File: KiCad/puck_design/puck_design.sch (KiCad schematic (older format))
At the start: 2 parts

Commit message: Changed library name
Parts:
- removed U?: ITG-3701, symbol library:ITG-3701
- removed U?: TE832-M1, symbol library:TE832-M1
- added U?: ITG-3701, symbol puck_library:ITG-3701
- added U?: TE832-M1, symbol puck_library:TE832-M1
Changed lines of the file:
@@
 EESchema Schematic File Version 4
+LIBS:puck_design-cache
 EELAYER 26 0
 EELAYER END
@@
 $EndDescr
 $Comp
-L library:ITG-3701 U?
-U 1 1 5BF4969E
-P 3500 3400
-F 0 "U?" H 4241 3496 50  0000 L CNN
-F 1 "ITG-3701" H 4241 3405 50  0000 L CNN
-F 2 "" H 3500 3400 50  0001 C CNN
-F 3 "" H 3500 3400 50  0001 C CNN
-	1    3500 3400
+L puck_library:ITG-3701 U?
+U 1 1 5BF49DCF
+P 3550 3200
+F 0 "U?" H 4291 3296 50  0000 L CNN
+F 1 "ITG-3701" H 4291 3205 50  0000 L CNN
+F 2 "" H 3550 3200 50  0001 C CNN
+F 3 "" H 3550 3200 50  0001 C CNN
+	1    3550 3200
 	1    0    0    -1
 $EndComp
 $Comp
-L library:TE832-M1 U?
-U 1 1 5BF496E3
-P 6000 3250
-F 0 "U?" H 5525 3565 50  0000 C CNN
-F 1 "TE832-M1" H 5525 3474 50  0000 C CNN
-F 2 "" H 5550 3550 50  0001 C CNN
-F 3 "" H 5550 3550 50  0001 C CNN
-	1    6000 3250
+L puck_library:TE832-M1 U?
+U 1 1 5BF49E68
+P 6000 3100
+F 0 "U?" H 5525 3415 50  0000 C CNN
+F 1 "TE832-M1" H 5525 3324 50  0000 C CNN
+F 2 "" H 5550 3400 50  0001 C CNN
+F 3 "" H 5550 3400 50  0001 C CNN
+	1    6000 3100
 	1    0    0    -1
 $EndComp

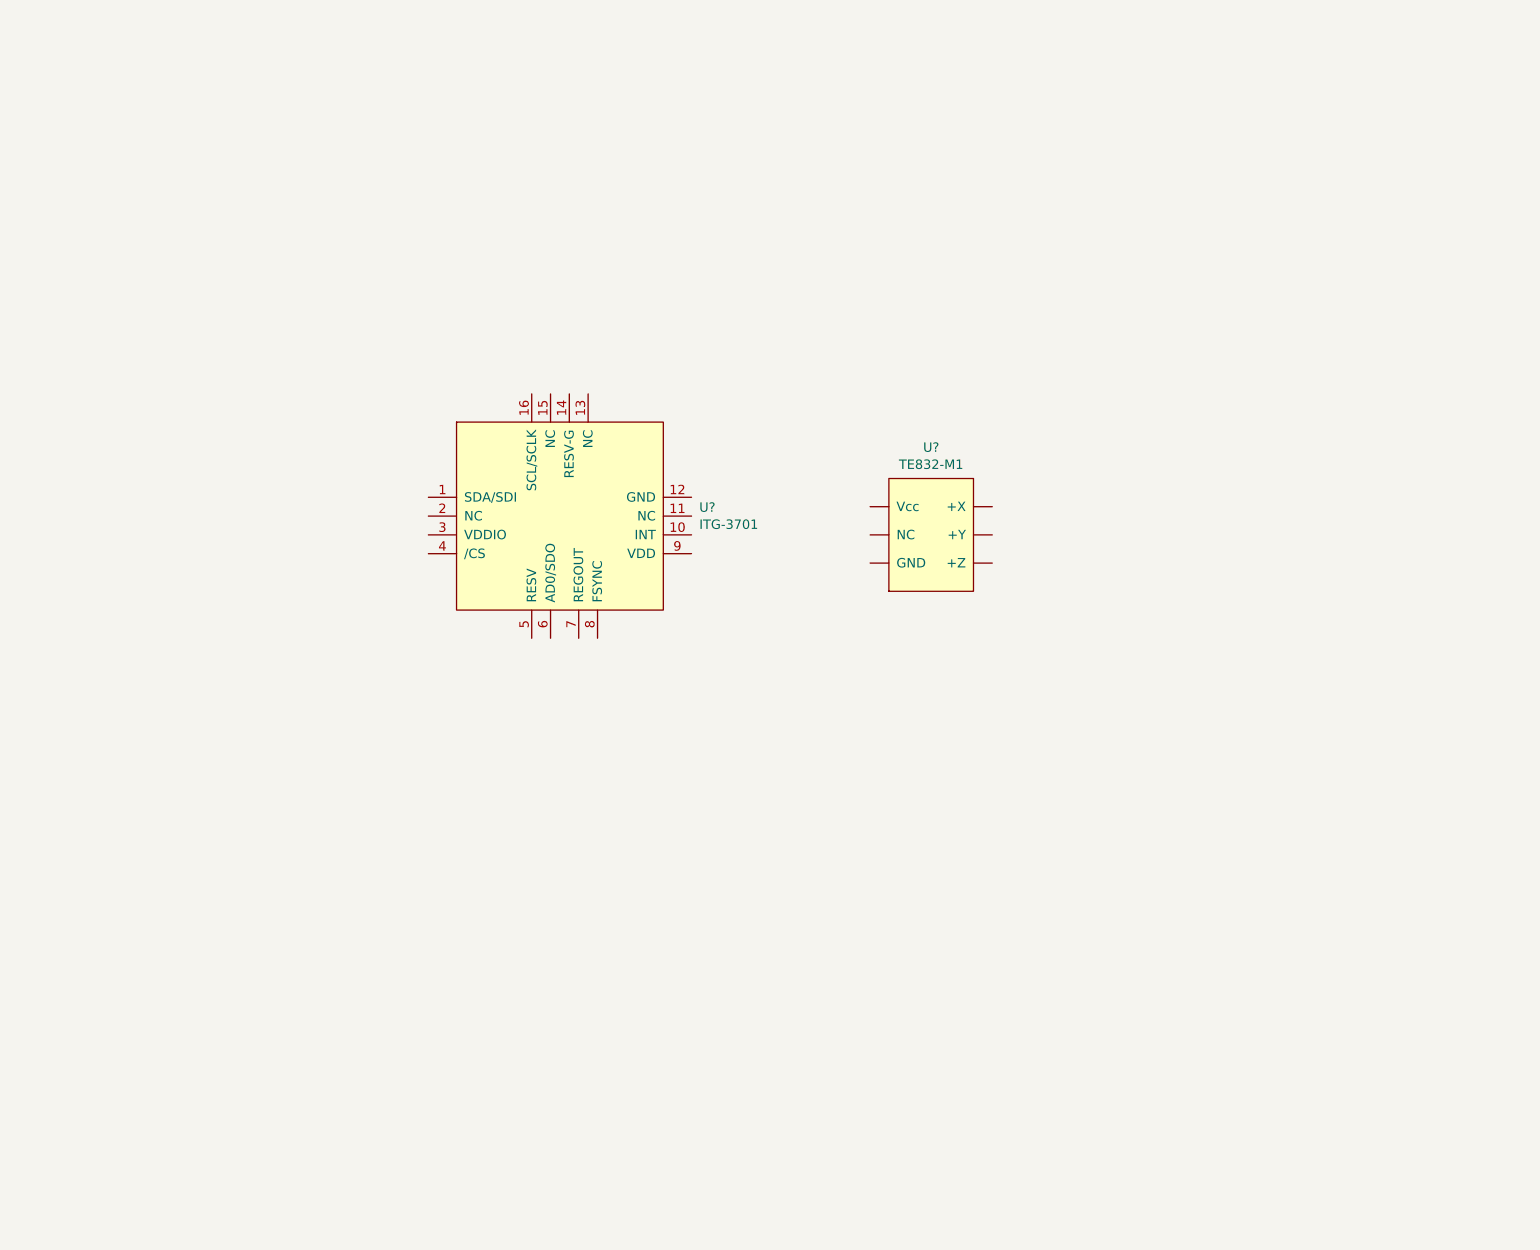
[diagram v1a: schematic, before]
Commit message: added connections according to config no 4
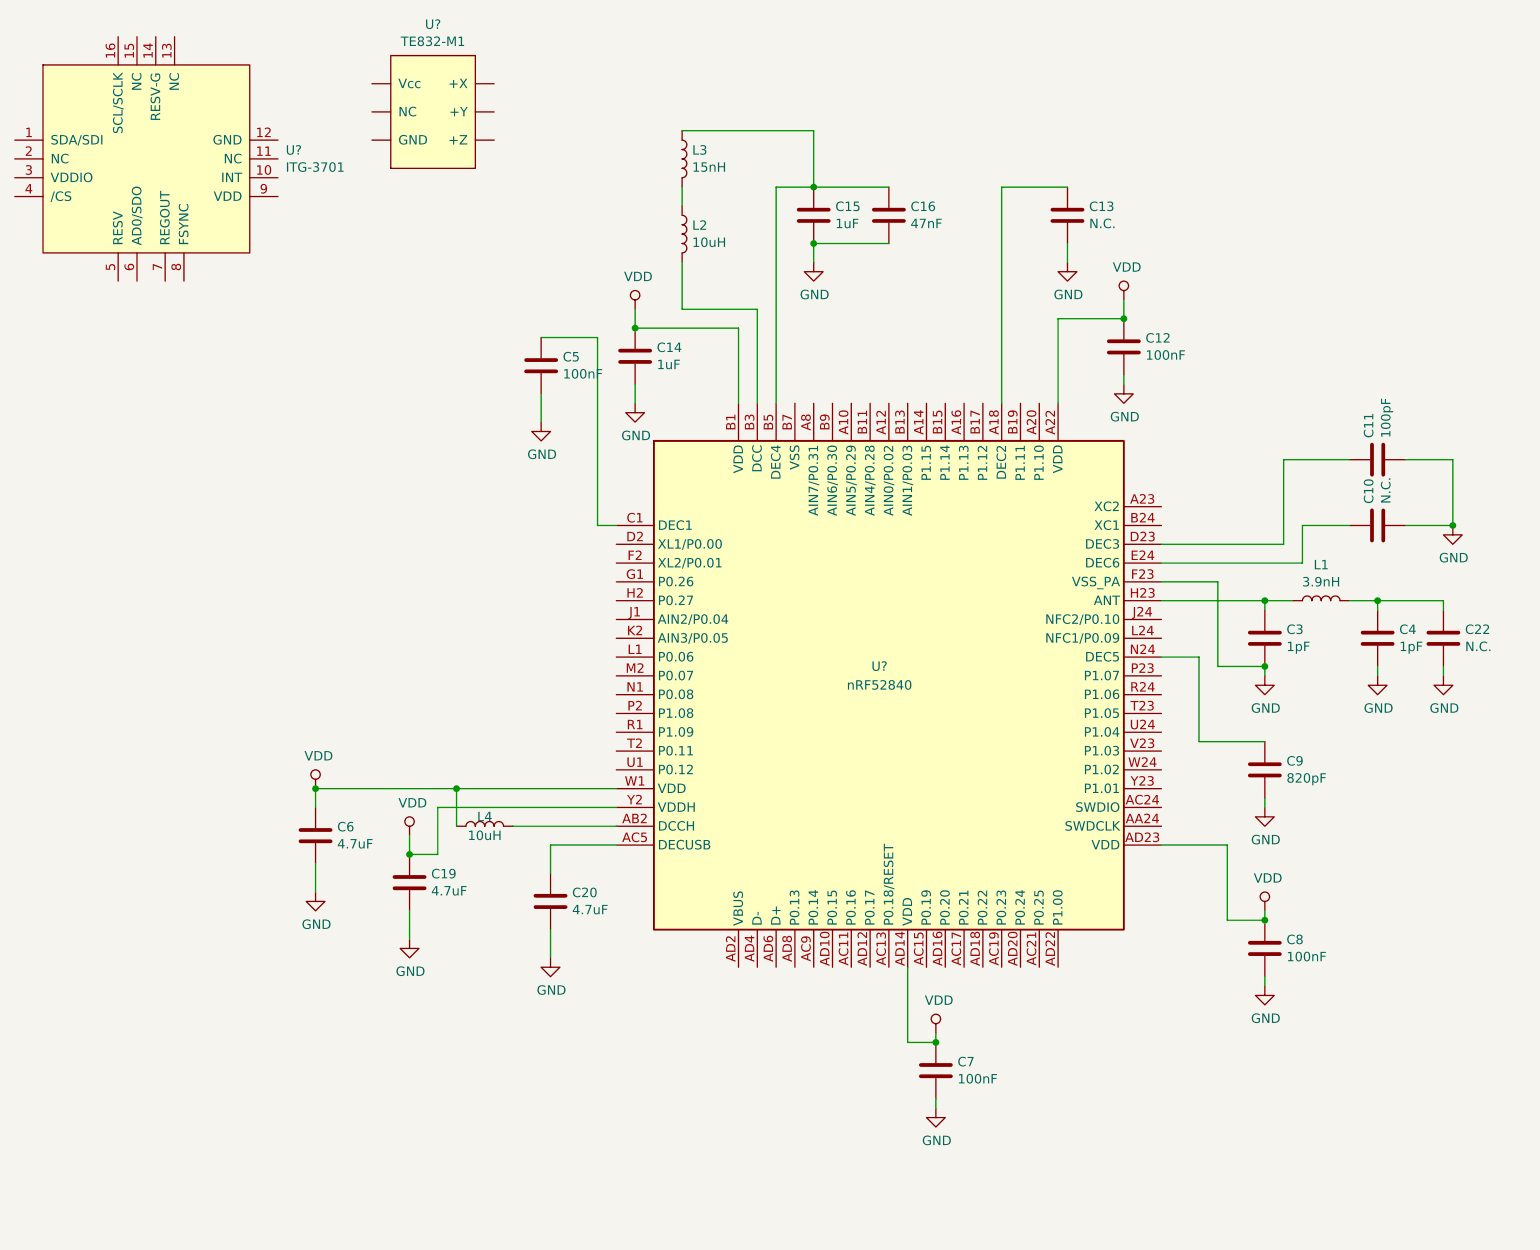
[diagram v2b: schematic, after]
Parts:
- added C10, C13, C22: N.C., symbol Device:C
- added C11: 100pF, symbol Device:C
- added C12, C5, C7, C8: 100nF, symbol Device:C
- added C14, C15: 1uF, symbol Device:C
- added C16: 47nF, symbol Device:C
- added C19, C20, C6: 4.7uF, symbol Device:C
- added C3, C4: 1pF, symbol Device:C
- added C9: 820pF, symbol Device:C
- added L1: 3.9nH, symbol Device:L
- added L2, L4: 10uH, symbol Device:L
- added L3: 15nH, symbol Device:L
- added U?: nRF52840, Package_DFN_QFN:Nordic_AQFN-73-1EP_7x7mm_P0.5mm, symbol puck_library:nRF52840
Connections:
- new net: C13.1, U?.A18 (DEC2)
- new net: L4.2, U?.AB2 (DCCH)
- new net: C20.1, U?.AC5 (DECUSB)
- new net: L2.2, U?.B3 (DCC)
- new net: C15.1, C16.1, L3.1, U?.B5 (DEC4)
- new net: C5.1, U?.C1 (DEC1)
- new net: C11.1, U?.D23 (DEC3)
- new net: C10.1, U?.E24 (DEC6)
- new net: C3.1, L1.1, U?.H23 (ANT)
- new net: C9.1, U?.N24 (DEC5)
- new net: C22.1, C4.1, L1.2
- new net: L2.1, L3.2
- new net GND: C10.2, C11.2, C12.2, C13.2, C14.2, C15.2, C16.2, C19.2, C20.2, C22.2, C3.2, C4.2, C5.2, C6.2, C7.2, C8.2, C9.2, U?.F23 (VSS_PA)
- new net VDD: C12.1, C14.1, C19.1, C6.1, C7.1, C8.1, L4.1, U?.A22 (VDD), U?.AD14 (VDD), U?.AD23 (VDD), U?.B1 (VDD), U?.W1 (VDD), U?.Y2 (VDDH)
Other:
- moved on the sheet: U?

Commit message: corrected errors
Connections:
- net GND: now also U?.B7 (VSS)
- net at C15.1, C16.1, L3.1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: now also C10.1, U?.E24 (DEC6)
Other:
- moved on the sheet: C11, C22
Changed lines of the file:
@@
 L Device:C C22
 U 1 1 5BF5900D
-P 8250 3800
-F 0 "C22" H 8365 3846 50  0000 L CNN
-F 1 "N.C." H 8365 3755 50  0000 L CNN
-F 2 "" H 8288 3650 50  0001 C CNN
-F 3 "~" H 8250 3800 50  0001 C CNN
-	1    8250 3800
+P 8350 3800
+F 0 "C22" H 8465 3846 50  0000 L CNN
+F 1 "N.C." H 8465 3755 50  0000 L CNN
+F 2 "" H 8388 3650 50  0001 C CNN
+F 3 "~" H 8350 3800 50  0001 C CNN
+	1    8350 3800
 	1    0    0    -1
 $EndComp
@@
 L Device:C C11
 U 1 1 5BF595A8
-P 7900 2850
-F 0 "C11" H 8015 2896 50  0000 L CNN
-F 1 "100pF" H 8015 2805 50  0000 L CNN
-F 2 "" H 7938 2700 50  0001 C CNN
-F 3 "~" H 7900 2850 50  0001 C CNN
-	1    7900 2850
+P 7900 2700
+F 0 "C11" V 8050 2650 50  0000 L CNN
+F 1 "100pF" V 7750 2600 50  0000 L CNN
+F 2 "" H 7938 2550 50  0001 C CNN
+F 3 "~" H 7900 2700 50  0001 C CNN
+	1    7900 2700
 	0    -1   -1   0
 $EndComp
@@
 U 1 1 5BF59610
 P 7900 3200
-F 0 "C10" H 8015 3246 50  0000 L CNN
-F 1 "N.C." H 8015 3155 50  0000 L CNN
+F 0 "C10" V 8050 3150 50  0000 L CNN
+F 1 "N.C." V 7750 3150 50  0000 L CNN
 F 2 "" H 7938 3050 50  0001 C CNN
 F 3 "~" H 7900 3200 50  0001 C CNN
@@
 L power:GND #PWR?
 U 1 1 5BF5F137
-P 8250 4000
-F 0 "#PWR?" H 8250 3750 50  0001 C CNN
-F 1 "GND" H 8255 3827 50  0000 C CNN
-F 2 "" H 8250 4000 50  0001 C CNN
-F 3 "" H 8250 4000 50  0001 C CNN
-	1    8250 4000
+P 8350 4000
+F 0 "#PWR?" H 8350 3750 50  0001 C CNN
+F 1 "GND" H 8355 3827 50  0000 C CNN
+F 2 "" H 8350 4000 50  0001 C CNN
+F 3 "" H 8350 4000 50  0001 C CNN
+	1    8350 4000
 	1    0    0    -1
 $EndComp
@@
 	6750 3300 7400 3300
 Wire Wire Line
-	7400 3300 7400 2850
-Wire Wire Line
-	7400 2850 7750 2850
-Wire Wire Line
 	6750 3400 7500 3400
 Wire Wire Line
@@
 $EndComp
 Wire Wire Line
-	8050 2850 8300 2850
-Wire Wire Line
-	8300 2850 8300 3200
-Wire Wire Line
 	8050 3200 8300 3200
-Connection ~ 8300 3200
 Wire Wire Line
 	6750 3600 7300 3600
@@
 	7900 3600 7900 3650
 Wire Wire Line
-	8250 3650 8250 3600
-Wire Wire Line
-	8250 3600 7900 3600
-Connection ~ 7900 3600
-Wire Wire Line
-	8250 3950 8250 4000
+	8350 3950 8350 4000
 Wire Wire Line
 	7900 3950 7900 4000
@@
 	2750 4850 2750 4950
 Connection ~ 2750 4950
+Wire Wire Line
+	5300 1400 5300 1100
+Wire Wire Line
+	5300 1100 7500 1100
+Wire Wire Line
+	7500 1100 7500 3200
+Connection ~ 5300 1400
+Connection ~ 7500 3200
+Wire Wire Line
+	4800 2550 4800 1700
+Wire Wire Line
+	4800 1700 4900 1700
+Wire Wire Line
+	7400 2700 7750 2700
+Wire Wire Line
+	7400 2700 7400 3300
+Wire Wire Line
+	8050 2700 8300 2700
+Wire Wire Line
+	8300 2700 8300 3200
+Connection ~ 8300 3200
+Wire Wire Line
+	8350 3650 8350 3600
+Wire Wire Line
+	8350 3600 7900 3600
+Connection ~ 7900 3600
 $EndSCHEMATC

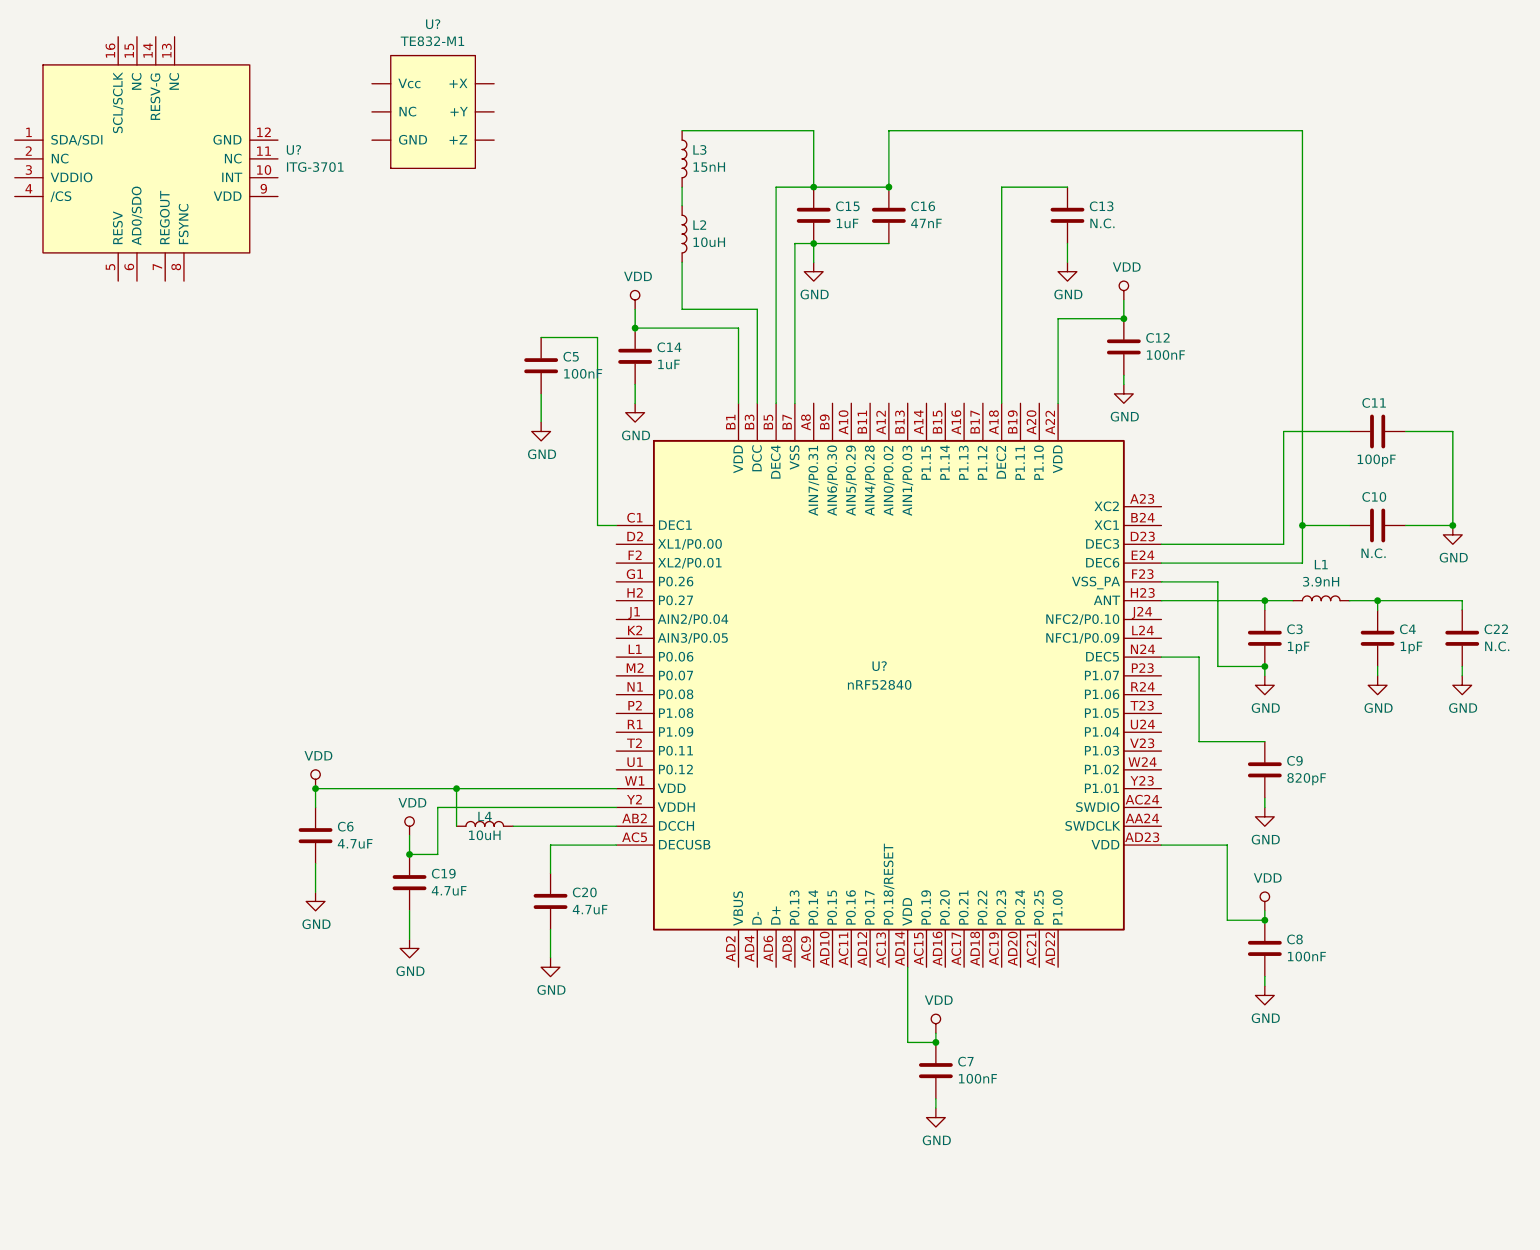
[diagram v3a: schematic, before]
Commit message: Added connections for accelerometer
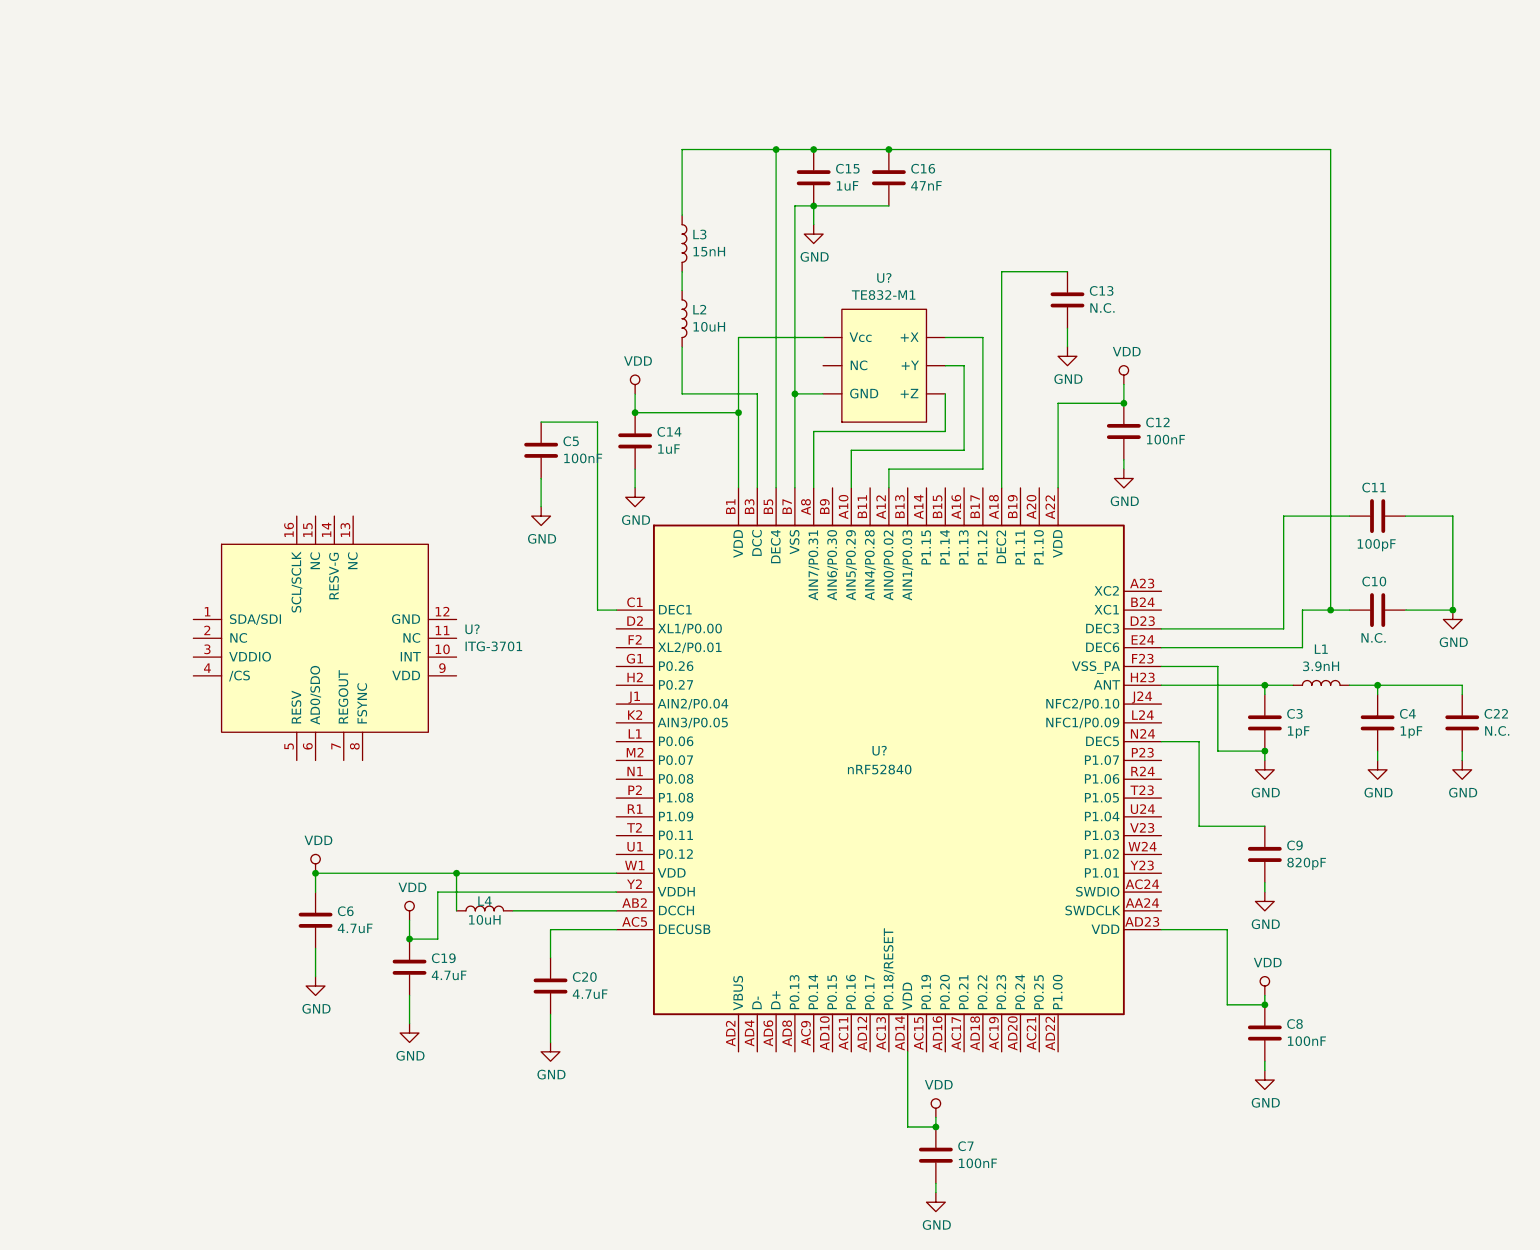
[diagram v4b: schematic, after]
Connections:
- net GND: now also U?.~ (Vcc)
- net VDD: now also U?.~ (Vcc)
- net at U?.A10 (AIN5/P0.29): now also U?.~ (Vcc)
- net at U?.A12 (AIN0/P0.02): now also U?.~ (Vcc)
- net at U?.A8 (AIN7/P0.31): now also U?.~ (Vcc)
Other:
- moved on the sheet: C10, C11, C12, C13, C14, C15, C16, C19, C20, C22, C3, C4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
